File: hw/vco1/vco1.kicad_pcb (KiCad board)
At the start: 4 copper layers, 30 x 128.5 mm, 83 parts, among them J1 Conn_02x08_Odd_Even, Q1 DNP, SW1 SW_SPDT, U1 SSI2131, U2 TL431BCDBZR, U4 TL072HxD, U5 TL072HxD

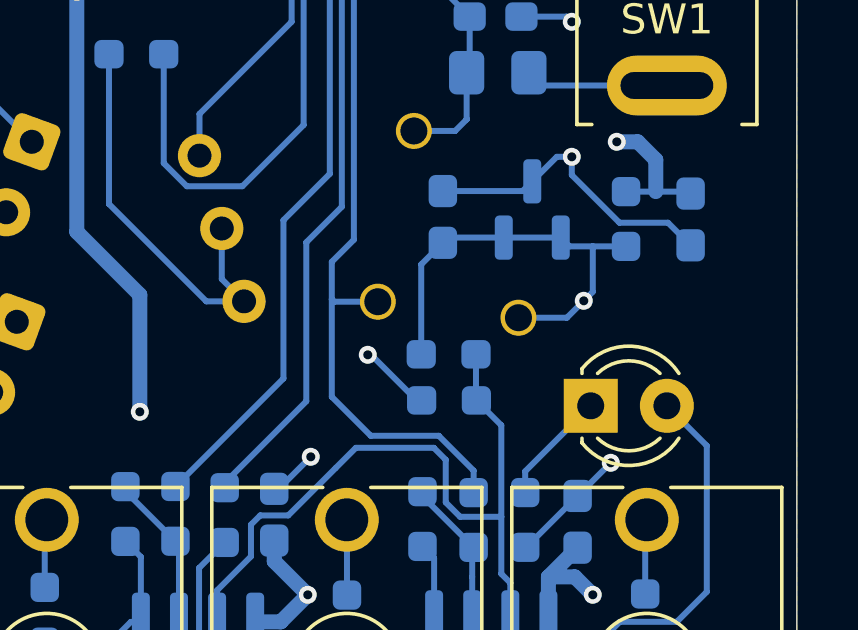
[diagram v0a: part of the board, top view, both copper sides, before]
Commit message: As built, fixed a couple of issues
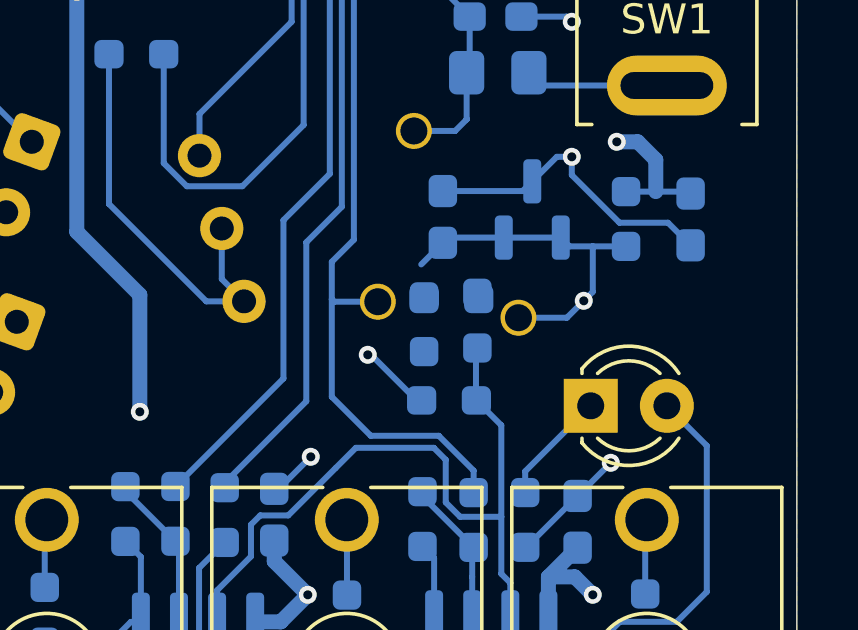
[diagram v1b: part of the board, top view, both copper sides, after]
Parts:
- added R34: 10k, Resistor_SMD:R_0603_1608Metric_Pad0.98x0.95mm_HandSolder, B.Cu at (93.5, 119.2)
- added R35: 10k, Resistor_SMD:R_0603_1608Metric_Pad0.98x0.95mm_HandSolder, B.Cu at (92.6, 120.1)
- R16: value 1M maybe? -> 1M
- R32, R33: value 20k -> 39k
- moved R32 1.48 mm to (94.4, 120.0), turned to -90 degrees
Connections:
- net /1.25V renamed /OPREF
- R32 pad 1: +2V5 -> Net-(R32-Pad1)
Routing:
- net +2V5: track 93.5 -> 90.5 mm
